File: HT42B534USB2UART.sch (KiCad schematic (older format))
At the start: 14 parts, among them J1 USB_A, J2 Conn_01x06, U1 HT42B534_8SOP

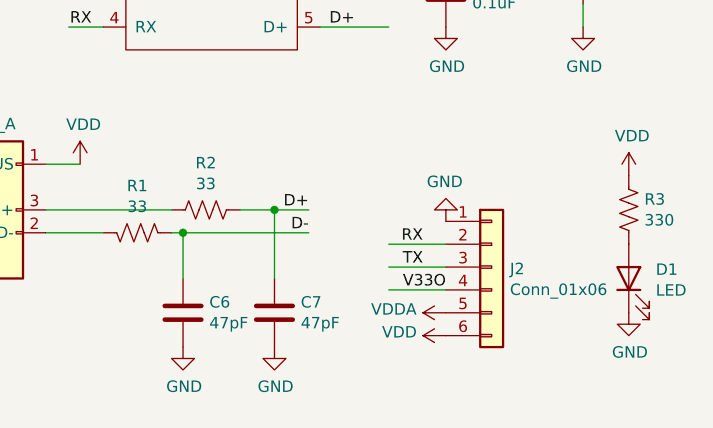
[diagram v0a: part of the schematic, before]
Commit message: Setup board parameters(track width, via size etc) and use filled Cu layers
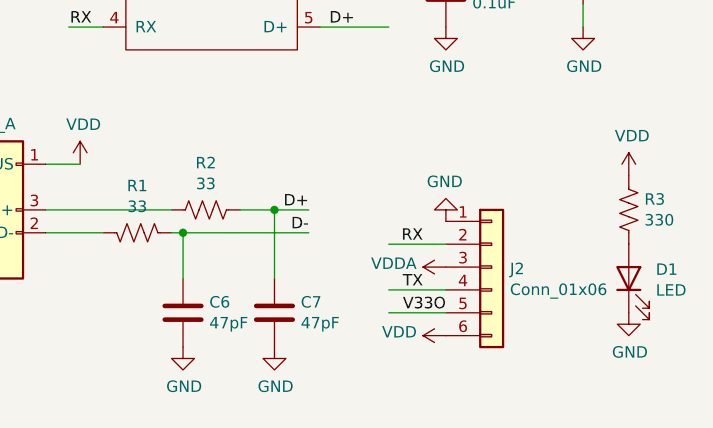
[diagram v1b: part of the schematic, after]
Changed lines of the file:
@@
 L power:VDDA #PWR0115
 U 1 1 5FECA433
-P 4250 3250
-F 0 "#PWR0115" H 4250 3100 50  0001 C CNN
-F 1 "VDDA" V 4265 3378 50  0000 L CNN
-F 2 "" H 4250 3250 50  0001 C CNN
-F 3 "" H 4250 3250 50  0001 C CNN
-	1    4250 3250
+P 4250 3050
+F 0 "#PWR0115" H 4250 2900 50  0001 C CNN
+F 1 "VDDA" V 4265 3178 50  0000 L CNN
+F 2 "" H 4250 3050 50  0001 C CNN
+F 3 "" H 4250 3050 50  0001 C CNN
+	1    4250 3050
 	0    -1   -1   0
 $EndComp
-Text Label 4150 3050 2    50   ~ 0
+Text Label 4150 3150 2    50   ~ 0
 TX
 Text Label 4150 2950 2    50   ~ 0
@@
 	1    0    0    -1
 $EndComp
-Text Label 4250 3150 2    50   ~ 0
+Text Label 4250 3250 2    50   ~ 0
 V33O
 Wire Wire Line
 	4000 2950 4250 2950
 Wire Wire Line
-	4000 3050 4250 3050
+	4000 3150 4250 3150
 Wire Wire Line
-	4000 3150 4250 3150
+	4000 3250 4250 3250
 $Comp
 L Connector_Generic:Conn_01x06 J2

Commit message: Add a conn01x03 for voltage selection
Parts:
- added J3: Conn_01x03, Connector_PinHeader_2.54mm:PinHeader_1x03_P2.54mm_Vertical, symbol Connector_Generic:Conn_01x03
- J2: value Conn_01x06 -> Conn_01x04; footprint Connector_PinHeader_2.54mm:PinHeader_1x06_P2.54mm_Horizontal -> Connector_PinHeader_2.54mm:PinHeader_1x04_P2.54mm_Horizontal; symbol Connector_Generic:Conn_01x06 -> Connector_Generic:Conn_01x04
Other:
- moved on the sheet: D1, R3
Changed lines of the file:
@@
 Connection ~ 1500 2850
-$Comp
-L power:VDD #PWR0114
-U 1 1 5FEC9C4E
-P 4250 3350
-F 0 "#PWR0114" H 4250 3200 50  0001 C CNN
-F 1 "VDD" V 4265 3477 50  0000 L CNN
-F 2 "" H 4250 3350 50  0001 C CNN
-F 3 "" H 4250 3350 50  0001 C CNN
-	1    4250 3350
-	0    -1   -1   0
-$EndComp
 $Comp
 L power:VDDA #PWR0115
 U 1 1 5FECA433
-P 4250 3050
-F 0 "#PWR0115" H 4250 2900 50  0001 C CNN
-F 1 "VDDA" V 4265 3178 50  0000 L CNN
-F 2 "" H 4250 3050 50  0001 C CNN
-F 3 "" H 4250 3050 50  0001 C CNN
-	1    4250 3050
+P 4100 3050
+F 0 "#PWR0115" H 4100 2900 50  0001 C CNN
+F 1 "VDDA" V 4115 3178 50  0000 L CNN
+F 2 "" H 4100 3050 50  0001 C CNN
+F 3 "" H 4100 3050 50  0001 C CNN
+	1    4100 3050
 	0    -1   -1   0
 $EndComp
-Text Label 4150 3150 2    50   ~ 0
+Text Label 4000 2950 2    50   ~ 0
 TX
-Text Label 4150 2950 2    50   ~ 0
+Text Label 4000 2850 2    50   ~ 0
 RX
 $Comp
 L power:GND #PWR0116
 U 1 1 5FECE8AD
-P 4250 2850
-F 0 "#PWR0116" H 4250 2600 50  0001 C CNN
-F 1 "GND" H 4255 2677 50  0000 C CNN
-F 2 "" H 4250 2850 50  0001 C CNN
-F 3 "" H 4250 2850 50  0001 C CNN
-	1    4250 2850
+P 4100 2750
+F 0 "#PWR0116" H 4100 2500 50  0001 C CNN
+F 1 "GND" H 4105 2577 50  0000 C CNN
+F 2 "" H 4100 2750 50  0001 C CNN
+F 3 "" H 4100 2750 50  0001 C CNN
+	1    4100 2750
 	-1   0    0    1
 $EndComp
@@
 L power:VDD #PWR0117
 U 1 1 5FED9097
-P 5050 2650
-F 0 "#PWR0117" H 5050 2500 50  0001 C CNN
-F 1 "VDD" H 5065 2823 50  0000 C CNN
-F 2 "" H 5050 2650 50  0001 C CNN
-F 3 "" H 5050 2650 50  0001 C CNN
-	1    5050 2650
+P 6250 2650
+F 0 "#PWR0117" H 6250 2500 50  0001 C CNN
+F 1 "VDD" H 6265 2823 50  0000 C CNN
+F 2 "" H 6250 2650 50  0001 C CNN
+F 3 "" H 6250 2650 50  0001 C CNN
+	1    6250 2650
 	1    0    0    -1
 $EndComp
@@
 L Device:R_US R3
 U 1 1 5FEDA0AA
-P 5050 2800
-F 0 "R3" H 5118 2846 50  0000 L CNN
-F 1 "330" H 5118 2755 50  0000 L CNN
-F 2 "Resistor_SMD:R_0603_1608Metric_Pad0.98x0.95mm_HandSolder" V 5090 2790 50  0001 C CNN
-F 3 "~" H 5050 2800 50  0001 C CNN
-	1    5050 2800
+P 6250 2800
+F 0 "R3" H 6318 2846 50  0000 L CNN
+F 1 "330" H 6318 2755 50  0000 L CNN
+F 2 "Resistor_SMD:R_0603_1608Metric_Pad0.98x0.95mm_HandSolder" V 6290 2790 50  0001 C CNN
+F 3 "~" H 6250 2800 50  0001 C CNN
+	1    6250 2800
 	1    0    0    -1
 $EndComp
@@
 L Device:LED D1
 U 1 1 5FEDB250
-P 5050 3100
-F 0 "D1" V 5089 2982 50  0000 R CNN
-F 1 "LED" V 4998 2982 50  0000 R CNN
-F 2 "Diode_SMD:D_0603_1608Metric_Pad1.05x0.95mm_HandSolder" H 5050 3100 50  0001 C CNN
-F 3 "~" H 5050 3100 50  0001 C CNN
-	1    5050 3100
+P 6250 3100
+F 0 "D1" V 6289 2982 50  0000 R CNN
+F 1 "LED" V 6198 2982 50  0000 R CNN
+F 2 "Diode_SMD:D_0603_1608Metric_Pad1.05x0.95mm_HandSolder" H 6250 3100 50  0001 C CNN
+F 3 "~" H 6250 3100 50  0001 C CNN
+	1    6250 3100
 	0    -1   -1   0
 $EndComp
@@
 L power:GND #PWR0118
 U 1 1 5FEDCB7C
-P 5050 3250
-F 0 "#PWR0118" H 5050 3000 50  0001 C CNN
-F 1 "GND" H 5055 3077 50  0000 C CNN
-F 2 "" H 5050 3250 50  0001 C CNN
-F 3 "" H 5050 3250 50  0001 C CNN
-	1    5050 3250
+P 6250 3250
+F 0 "#PWR0118" H 6250 3000 50  0001 C CNN
+F 1 "GND" H 6255 3077 50  0000 C CNN
+F 2 "" H 6250 3250 50  0001 C CNN
+F 3 "" H 6250 3250 50  0001 C CNN
+	1    6250 3250
 	1    0    0    -1
 $EndComp
@@
 	1    0    0    -1
 $EndComp
-Text Label 4250 3250 2    50   ~ 0
+Text Label 5200 3100 2    50   ~ 0
 V33O
 Wire Wire Line
-	4000 2950 4250 2950
-Wire Wire Line
-	4000 3150 4250 3150
-Wire Wire Line
-	4000 3250 4250 3250
+	4950 3100 5200 3100
 $Comp
-L Connector_Generic:Conn_01x06 J2
-U 1 1 5FEC8B41
-P 4450 3050
-F 0 "J2" H 4530 3042 50  0000 L CNN
-F 1 "Conn_01x06" H 4530 2951 50  0000 L CNN
-F 2 "Connector_PinHeader_2.54mm:PinHeader_1x06_P2.54mm_Horizontal" H 4450 3050 50  0001 C CNN
-F 3 "~" H 4450 3050 50  0001 C CNN
-	1    4450 3050
+L Connector_Generic:Conn_01x03 J3
+U 1 1 5FF92187
+P 5400 3000
+F 0 "J3" H 5480 3042 50  0000 L CNN
+F 1 "Conn_01x03" H 5480 2951 50  0000 L CNN
+F 2 "Connector_PinHeader_2.54mm:PinHeader_1x03_P2.54mm_Vertical" H 5400 3000 50  0001 C CNN
+F 3 "~" H 5400 3000 50  0001 C CNN
+	1    5400 3000
 	1    0    0    -1
 $EndComp
+$Comp
+L power:VDD #PWR0114
+U 1 1 5FF97B02
+P 5200 2900
+F 0 "#PWR0114" H 5200 2750 50  0001 C CNN
+F 1 "VDD" V 5215 3027 50  0000 L CNN
+F 2 "" H 5200 2900 50  0001 C CNN
+F 3 "" H 5200 2900 50  0001 C CNN
+	1    5200 2900
+	0    -1   -1   0
+$EndComp
+$Comp
+L power:VDDA #PWR0120
+U 1 1 5FF98919
+P 5200 3000
+F 0 "#PWR0120" H 5200 2850 50  0001 C CNN
+F 1 "VDDA" V 5215 3128 50  0000 L CNN
+F 2 "" H 5200 3000 50  0001 C CNN
+F 3 "" H 5200 3000 50  0001 C CNN
+	1    5200 3000
+	0    -1   -1   0
+$EndComp
+$Comp
+L Connector_Generic:Conn_01x04 J2
+U 1 1 5FEC8B41
+P 4300 2850
+F 0 "J2" H 4380 2842 50  0000 L CNN
+F 1 "Conn_01x04" H 4380 2751 50  0000 L CNN
+F 2 "Connector_PinHeader_2.54mm:PinHeader_1x04_P2.54mm_Horizontal" H 4300 2850 50  0001 C CNN
+F 3 "~" H 4300 2850 50  0001 C CNN
+	1    4300 2850
+	1    0    0    -1
+$EndComp
+Wire Wire Line
+	3850 2850 4100 2850
+Wire Wire Line
+	3850 2950 4100 2950
 $EndSCHEMATC

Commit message: Use custom symbol library
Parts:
- J1: symbol Connector:USB_A_DEVICE -> Custom:USB_A_DEVICE
- U1: symbol Interface_USB:HT42B534_8SOP -> Custom:HT42B534_8SOP
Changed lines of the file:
@@
 $EndDescr
 $Comp
-L Interface_USB:HT42B534_8SOP U1
+L Custom:HT42B534_8SOP U1
 U 1 1 5FE8F8C2
 P 3250 1900
@@
 	1500 1650 1500 1450
 $Comp
-L Connector:USB_A_DEVICE J1
+L Custom:USB_A_DEVICE J1
 U 1 1 5FEA1885
 P 2200 2800

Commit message: Minor update
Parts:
- J1: Product (none) -> https://item.szlcsc.com/98530.html
- U1: Product (none) -> https://item.szlcsc.com/504007.html
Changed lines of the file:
@@
 F 2 "Package_SO:SOP-8_3.9x4.9mm_P1.27mm" H 2900 2400 50  0001 C CNN
 F 3 "https://www.holtek.com/documents/10179/116711/HT42B534-xv110.pdf" H 2900 2400 50  0001 C CNN
+F 4 "https://item.szlcsc.com/504007.html" H 3250 1900 50  0001 C CNN "Product"
 	1    3250 1900
 	1    0    0    -1
@@
 F 2 "Connector_USB:USB_A_CNCTech_1001-011-01101_Horizontal" H 2350 2750 50  0001 C CNN
 F 3 " ~" H 2350 2750 50  0001 C CNN
+F 4 "https://item.szlcsc.com/98530.html" H 2200 2800 50  0001 C CNN "Product"
 	1    2200 2800
 	1    0    0    -1
